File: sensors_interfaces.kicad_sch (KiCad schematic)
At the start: 31 parts, among them IC601 STK8321, IC602 SP3485EN-L_TR, IC603 WM8782SEDS_RV_C323842, IC604 CS4344-CZZ, IC605 MCP9700AT-E_TT, X601 KF2EDGR-3.81-3P, X602 PJ-327C-4A, X603 PJ-327C-4A

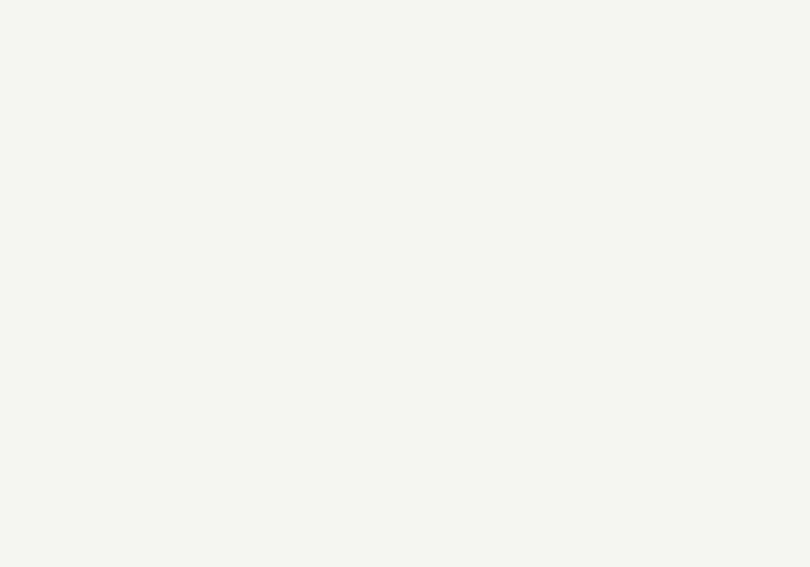
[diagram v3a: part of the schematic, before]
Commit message: move IMU to interfaces page
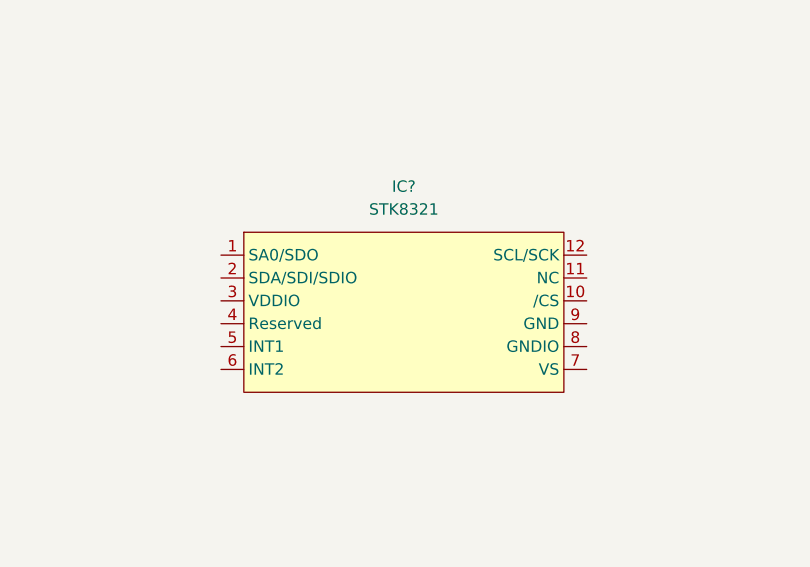
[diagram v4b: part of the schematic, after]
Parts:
- added IC?: STK8321, LGA-12_L2.0-W2.0-P0.50-TR, symbol eduboardv2:STK8321
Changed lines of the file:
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@@
     (pin "2")
+  )
+  (symbol (lib_id "eduboardv2:STK8321") (at 187.96 153.67 0) (unit 1)
+    (in_bom yes) (on_board yes) (fields_autoplaced)
+    (property "Reference" "IC?" (id 0) (at 187.96 139.7 0))
+    (property "Value" "STK8321" (id 1) (at 187.96 142.24 0))
+    (property "Footprint" "LGA-12_L2.0-W2.0-P0.50-TR" (id 2) (at 187.96 167.64 0)
+      (effects (font (size 1.27 1.27)) hide)
+    )
+    (property "Datasheet" "" (id 3) (at 187.96 153.67 0)
+      (effects (font (size 1.27 1.27)) hide)
+    )
+    (property "Manufacturer" "SENSORTEK(昇佳)" (id 4) (at 187.96 172.72 0)
+      (effects (font (size 1.27 1.27)) hide)
+    )
+    (property "LCSC Part" "C966924" (id 5) (at 187.96 175.26 0)
+      (effects (font (size 1.27 1.27)) hide)
+    )
+    (property "JLC Part" "Extended Part" (id 6) (at 187.96 177.8 0)
+      (effects (font (size 1.27 1.27)) hide)
+    )
+    (property "MPN" "STK8321" (id 7) (at 187.96 165.1 0)
+      (effects (font (size 1.27 1.27)) hide)
+    )
+    (pin "1")
+    (pin "10")
+    (pin "11")
+    (pin "12")
+    (pin "2")
+    (pin "3")
+    (pin "4")
+    (pin "5")
+    (pin "6")
+    (pin "7")
+    (pin "8")
+    (pin "9")
   )
   (symbol (lib_name "CL05B104KB54PNC_2") (lib_id "eduboardv2:CL05B104KB54PNC") (at 189.23 74.93 90) (unit 1)

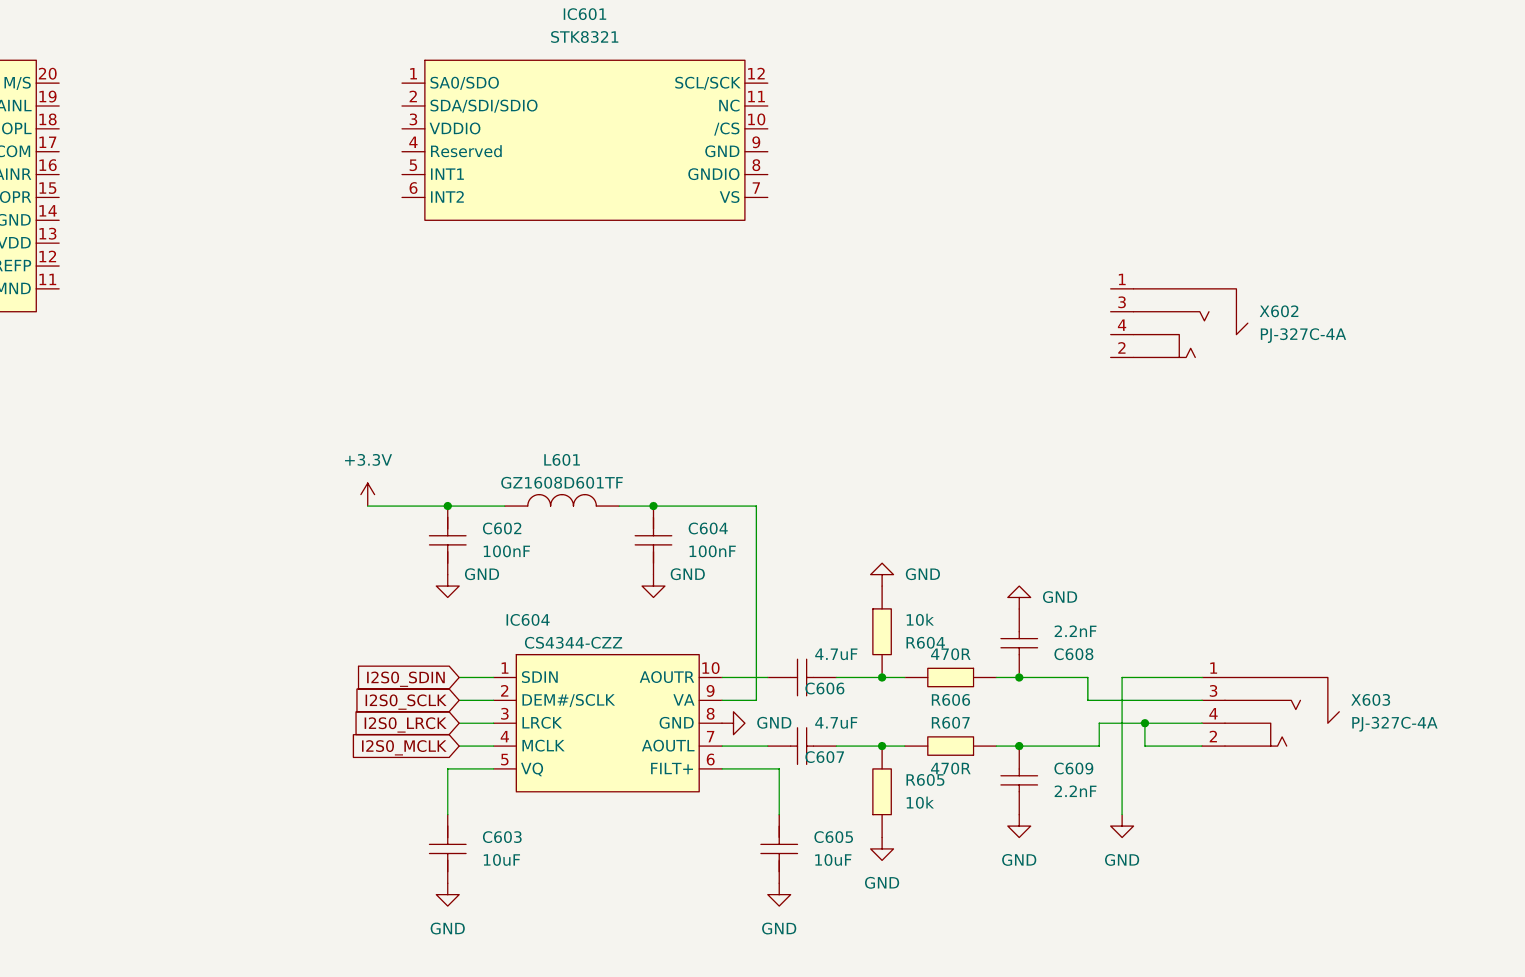
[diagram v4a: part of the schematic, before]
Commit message: move Audio-Connectors to connectors page
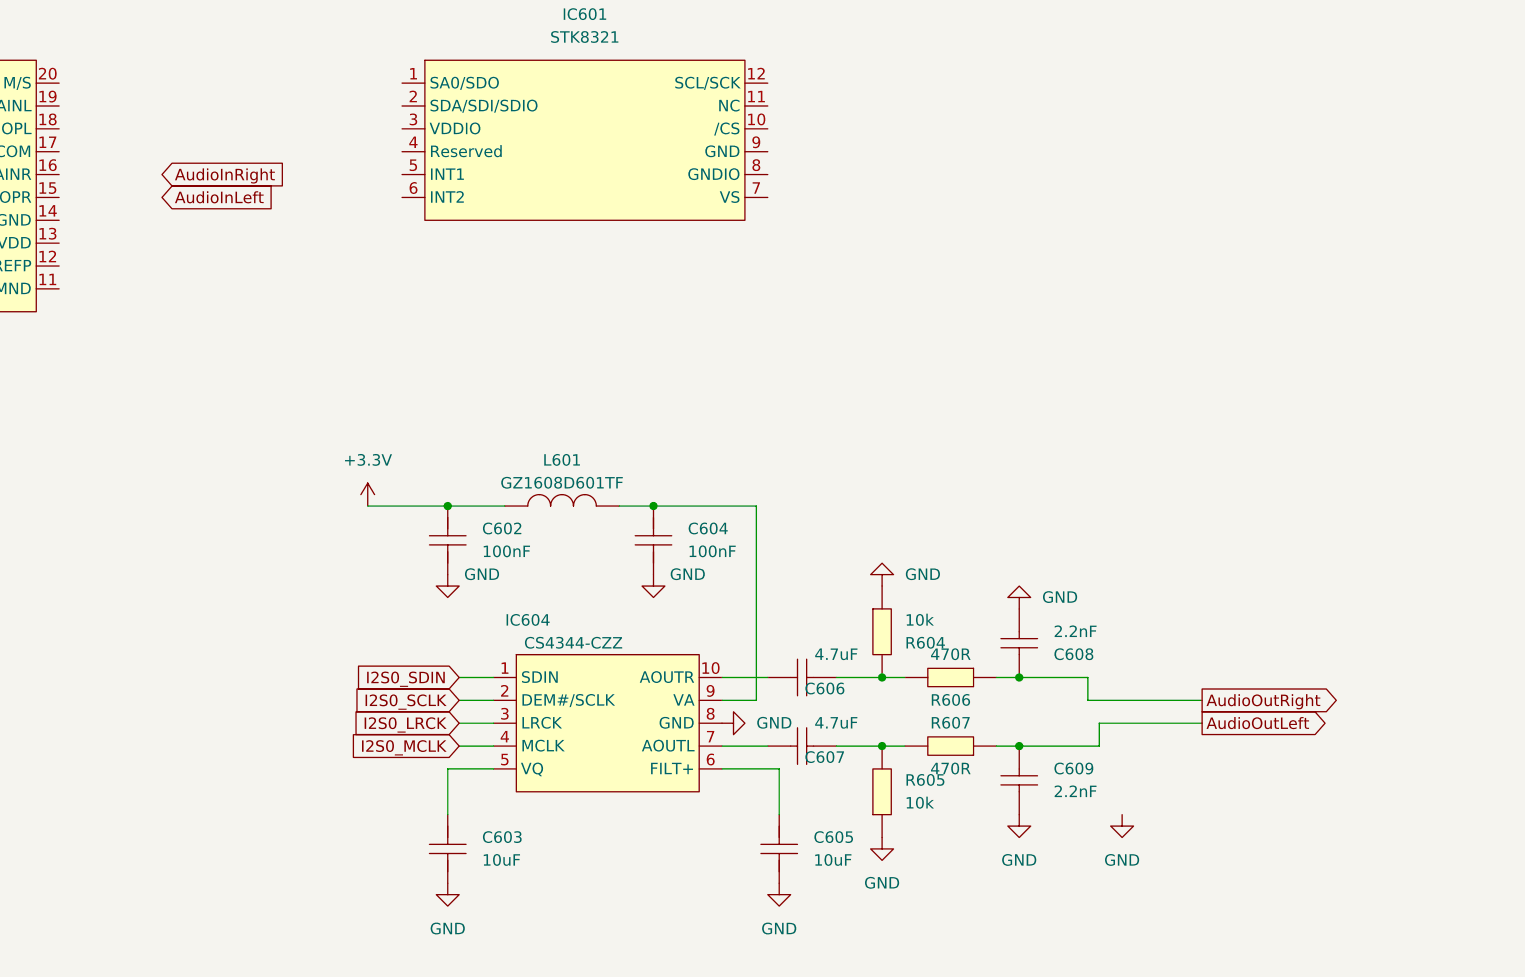
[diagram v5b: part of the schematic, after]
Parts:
- removed X602, X603: PJ-327C-4A, AUDIO-SMD_PJ-327C-4A, symbol eduboardv2:PJ-327C-4A
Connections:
- net AudioOutRight: now reaches C608.2, R606.1
- net AudioOutLeft: now reaches C609.2, R607.1
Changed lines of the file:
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@@
   (junction (at 57.15 154.94) (diameter 0) (color 0 0 0 0)
   )
-  (junction (at 243.84 95.25) (diameter 0) (color 0 0 0 0)
-  )
   (junction (at 43.18 124.46) (diameter 0) (color 0 0 0 0)
   )
@@
     (stroke (width 0) (type default) (color 0 0 0 0))
   )
-  (wire (pts (xy 250.19 95.25) (xy 243.84 95.25))
+  (wire (pts (xy 238.76 95.25) (xy 250.19 95.25))
     (stroke (width 0) (type default) (color 0 0 0 0))
   )
@@
     (stroke (width 0) (type default) (color 0 0 0 0))
   )
-  (wire (pts (xy 243.84 97.79) (xy 243.84 95.25))
-    (stroke (width 0) (type default) (color 0 0 0 0))
-  )
   (wire (pts (xy 196.85 90.17) (xy 201.93 90.17))
     (stroke (width 0) (type default) (color 0 0 0 0))
@@
     (stroke (width 0) (type default) (color 0 0 0 0))
   )
-  (wire (pts (xy 241.3 90.17) (xy 241.3 105.41))
-    (stroke (width 0) (type default) (color 0 0 0 0))
-  )
   (wire (pts (xy 50.8 132.08) (xy 50.8 124.46))
     (stroke (width 0) (type default) (color 0 0 0 0))
@@
     (stroke (width 0) (type default) (color 0 0 0 0))
   )
-  (wire (pts (xy 243.84 95.25) (xy 238.76 95.25))
-    (stroke (width 0) (type default) (color 0 0 0 0))
-  )
   (wire (pts (xy 33.02 175.26) (xy 35.56 175.26))
     (stroke (width 0) (type default) (color 0 0 0 0))
@@
   )
   (wire (pts (xy 167.64 97.79) (xy 171.45 97.79))
-    (stroke (width 0) (type default) (color 0 0 0 0))
-  )
-  (wire (pts (xy 250.19 90.17) (xy 241.3 90.17))
-    (stroke (width 0) (type default) (color 0 0 0 0))
-  )
-  (wire (pts (xy 250.19 97.79) (xy 243.84 97.79))
     (stroke (width 0) (type default) (color 0 0 0 0))
   )
@@
     )
   )
+  (global_label "AudioOutLeft" (shape output) (at 250.19 95.25 0) (fields_autoplaced)
+    (effects (font (size 1.27 1.27)) (justify left))
+    (property "Intersheet References" "${INTERSHEET_REFS}" (id 0) (at 264.5169 95.1706 0)
+      (effects (font (size 1.27 1.27)) (justify left) hide)
+    )
+  )
   (global_label "RS485_DE" (shape input) (at 33.02 175.26 180) (fields_autoplaced)
     (effects (font (size 1.27 1.27)) (justify right))
@@
     )
   )
+  (global_label "AudioInLeft" (shape input) (at 134.62 36.83 0) (fields_autoplaced)
+    (effects (font (size 1.27 1.27)) (justify left))
+    (property "Intersheet References" "${INTERSHEET_REFS}" (id 0) (at 147.4955 36.7506 0)
+      (effects (font (size 1.27 1.27)) (justify left) hide)
+    )
+  )
   (global_label "UART_RS485_TX" (shape input) (at 33.02 179.07 180) (fields_autoplaced)
     (effects (font (size 1.27 1.27)) (justify right))
@@
     )
   )
+  (global_label "AudioInRight" (shape input) (at 134.62 34.29 0) (fields_autoplaced)
+    (effects (font (size 1.27 1.27)) (justify left))
+    (property "Intersheet References" "${INTERSHEET_REFS}" (id 0) (at 148.826 34.2106 0)
+      (effects (font (size 1.27 1.27)) (justify left) hide)
+    )
+  )
   (global_label "USB_UART0_TX" (shape output) (at 43.18 100.33 180) (fields_autoplaced)
     (effects (font (size 1.27 1.27)) (justify right))
@@
     (property "Intersheet References" "${INTERSHEET_REFS}" (id 0) (at 155.0064 97.7106 0)
       (effects (font (size 1.27 1.27)) (justify right) hide)
+    )
+  )
+  (global_label "AudioOutRight" (shape output) (at 250.19 92.71 0) (fields_autoplaced)
+    (effects (font (size 1.27 1.27)) (justify left))
+    (property "Intersheet References" "${INTERSHEET_REFS}" (id 0) (at 265.8474 92.6306 0)
+      (effects (font (size 1.27 1.27)) (justify left) hide)
     )
   )
@@
     (pin "1")
     (pin "2")
-  )
-  (symbol (lib_name "PJ-327C-4A_1") (lib_id "eduboardv2:PJ-327C-4A") (at 246.38 49.53 0) (mirror y) (unit 1)
-    (in_bom yes) (on_board yes) (fields_autoplaced)
-    (property "Reference" "X602" (id 0) (at 256.54 49.5299 0)
-      (effects (font (size 1.27 1.27)) (justify right))
-    )
-    (property "Value" "PJ-327C-4A" (id 1) (at 256.54 52.0699 0)
-      (effects (font (size 1.27 1.27)) (justify right))
-    )
-    (property "Footprint" "AUDIO-SMD_PJ-327C-4A" (id 2) (at 246.38 62.23 0)
-      (effects (font (size 1.27 1.27)) hide)
-    )
-    (property "Datasheet" "https://lcsc.com/product-detail/Audio-Connectors_PJ-327C-4A_C145813.html" (id 3) (at 246.38 67.31 0)
-      (effects (font (size 1.27 1.27)) hide)
-    )
-    (property "Manufacturer" "HRO" (id 4) (at 246.38 69.85 0)
-      (effects (font (size 1.27 1.27)) hide)
-    )
-    (property "LCSC Part" "C145813" (id 5) (at 246.38 72.39 0)
-      (effects (font (size 1.27 1.27)) hide)
-    )
-    (property "JLC Part" "Extended Part" (id 6) (at 246.38 74.93 0)
-      (effects (font (size 1.27 1.27)) hide)
-    )
-    (property "MPN" "PJ-327C-4A" (id 7) (at 246.38 59.69 0)
-      (effects (font (size 1.27 1.27)) hide)
-    )
-    (pin "1")
-    (pin "2")
-    (pin "3")
-    (pin "4")
   )
   (symbol (lib_id "eduboardv2:CL10A475KO8NNNC") (at 205.74 90.17 0) (unit 1)
@@
     (pin "9")
   )
-  (symbol (lib_id "eduboardv2:PJ-327C-4A") (at 256.54 92.71 0) (mirror y) (unit 1)
-    (in_bom yes) (on_board yes) (fields_autoplaced)
-    (property "Reference" "X603" (id 0) (at 266.7 92.7099 0)
-      (effects (font (size 1.27 1.27)) (justify right))
-    )
-    (property "Value" "PJ-327C-4A" (id 1) (at 266.7 95.2499 0)
-      (effects (font (size 1.27 1.27)) (justify right))
-    )
-    (property "Footprint" "AUDIO-SMD_PJ-327C-4A" (id 2) (at 256.54 105.41 0)
-      (effects (font (size 1.27 1.27)) hide)
-    )
-    (property "Datasheet" "https://lcsc.com/product-detail/Audio-Connectors_PJ-327C-4A_C145813.html" (id 3) (at 256.54 110.49 0)
-      (effects (font (size 1.27 1.27)) hide)
-    )
-    (property "Manufacturer" "HRO" (id 4) (at 256.54 113.03 0)
-      (effects (font (size 1.27 1.27)) hide)
-    )
-    (property "LCSC Part" "C145813" (id 5) (at 256.54 115.57 0)
-      (effects (font (size 1.27 1.27)) hide)
-    )
-    (property "JLC Part" "Extended Part" (id 6) (at 256.54 118.11 0)
-      (effects (font (size 1.27 1.27)) hide)
-    )
-    (property "MPN" "PJ-327C-4A" (id 7) (at 256.54 102.87 0)
-      (effects (font (size 1.27 1.27)) hide)
-    )
-    (pin "1")
-    (pin "2")
-    (pin "3")
-    (pin "4")
-  )
   (symbol (lib_name "0402CG220J500NT_2") (lib_id "eduboardv2:0402CG220J500NT") (at 50.8 135.89 90) (unit 1)
